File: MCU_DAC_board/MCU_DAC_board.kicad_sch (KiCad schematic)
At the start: 1 part, among them U1 ADAU1966AWBSTZ

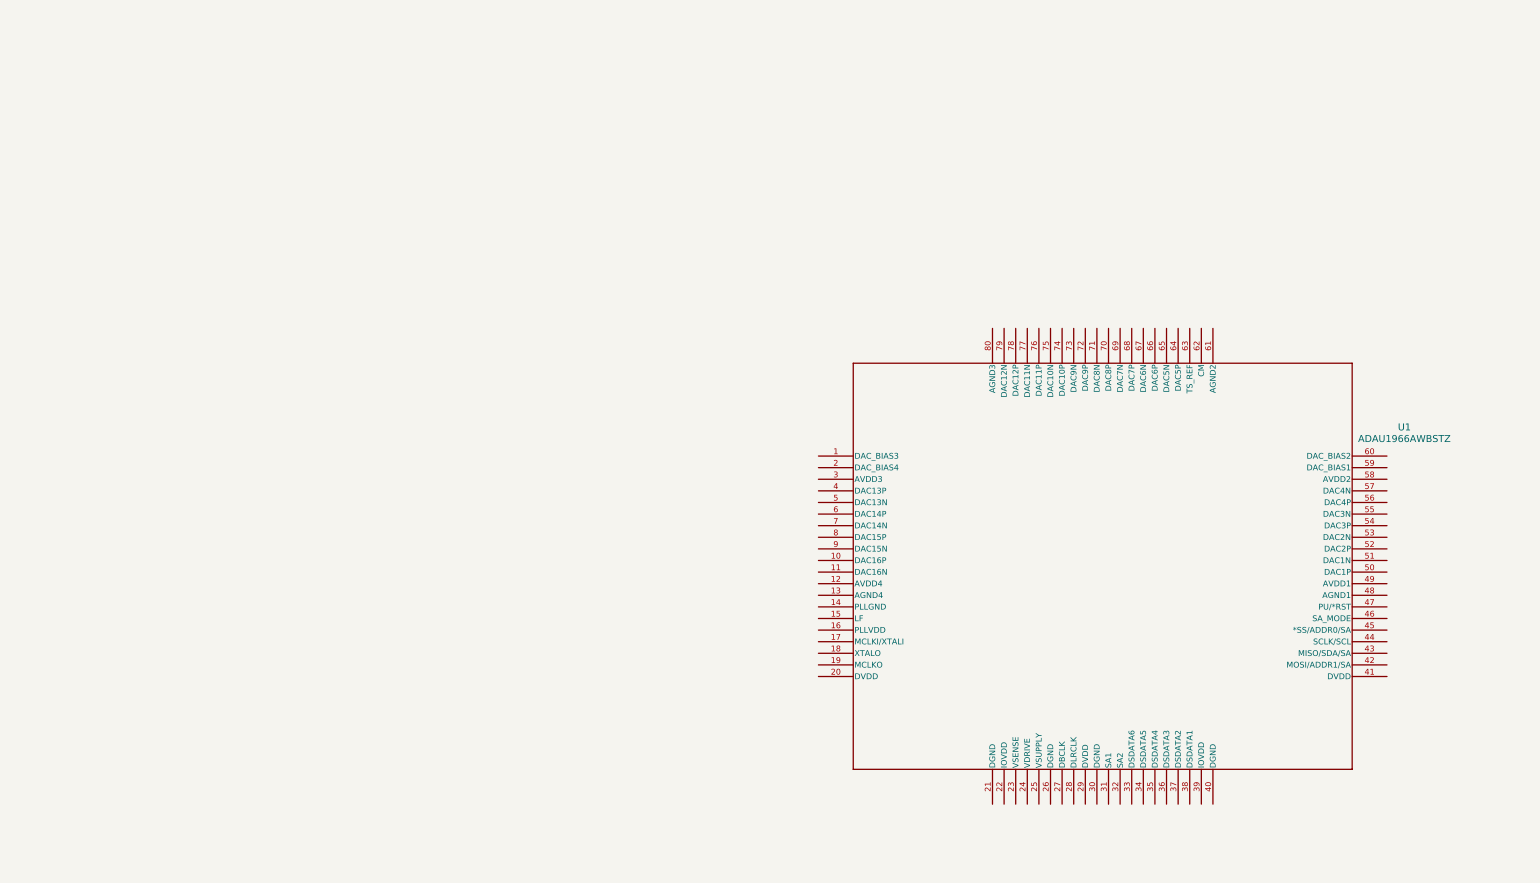
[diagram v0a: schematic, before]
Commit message: Added MCU dev board, connected power pins of DAC
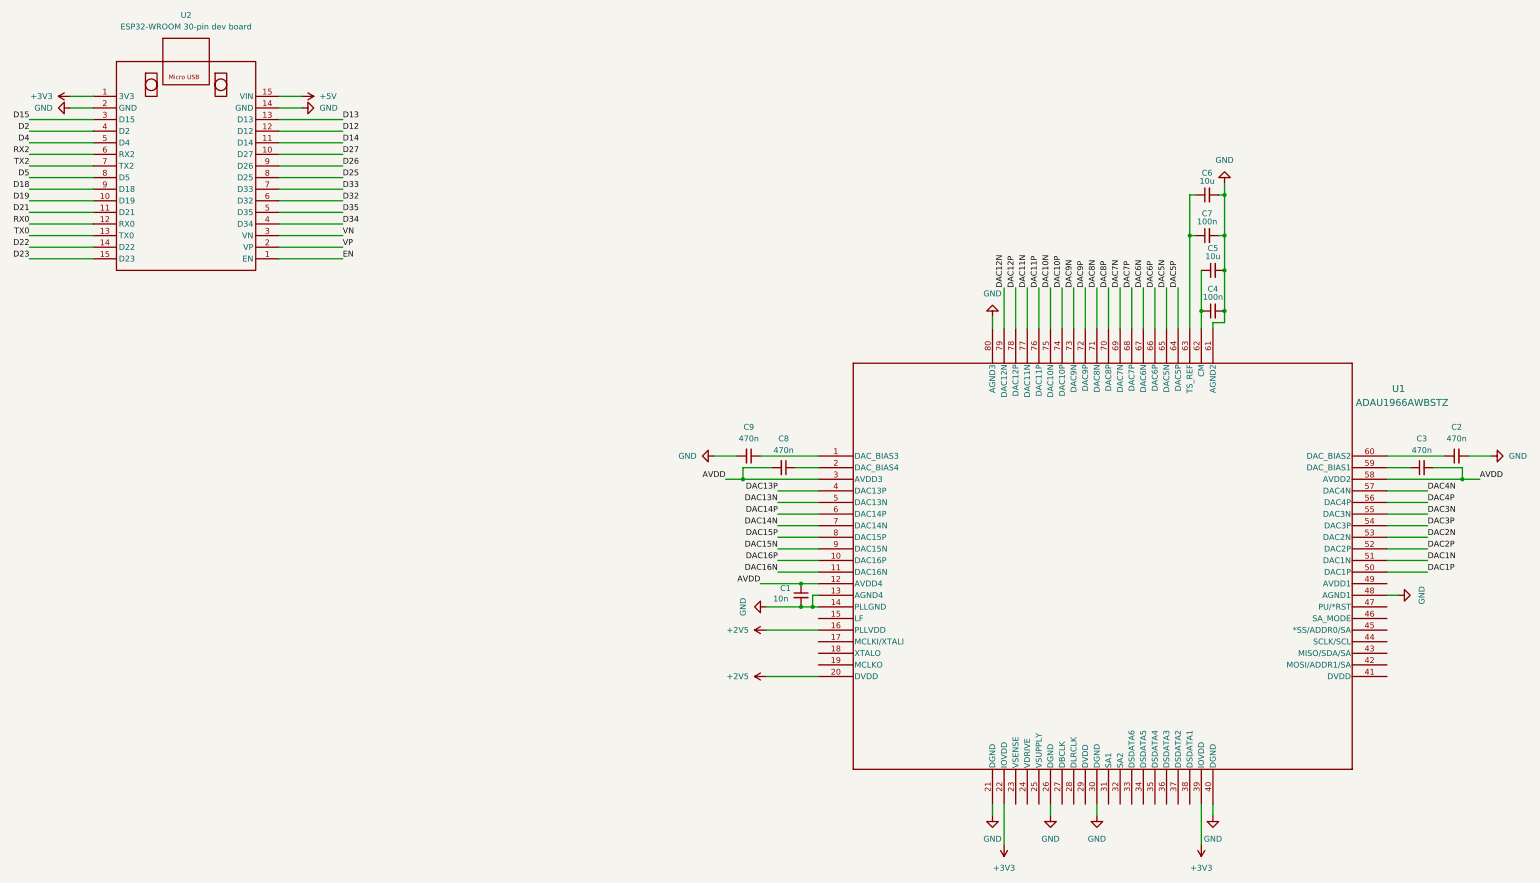
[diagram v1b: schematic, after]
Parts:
- added C1: 10n, symbol Device:C_Small
- added C2, C3, C8, C9: 470n, symbol Device:C_Small
- added C4, C7: 100n, symbol Device:C_Small
- added C5, C6: 10u, symbol Device:C_Small
- added U2: ESP32-WROOM 30-pin dev board, project_lib:ESP32-WROOM-30-DEVBOARD, symbol project_lib:ESP32-WROOM 30-pin dev board
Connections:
- net at U1.1 (DAC_BIAS3): now also C9.1
- net DAC16P: now reaches U1.10 (DAC16P)
- net DAC16N: now reaches U1.11 (DAC16N)
- net AVDD: now reaches U1.12 (AVDD4)
- net AVDD: now also U1.3 (AVDD3), U1.58 (AVDD2), C1.1, C3.2, C8.2
- net GND: now reaches U1.13 (AGND4)
- net GND: now also U1.14 (PLLGND), U1.21 (DGND), U1.26 (DGND), U1.30 (DGND), U1.40 (DGND), U1.48 (AGND1), U1.61 (AGND2), U1.80 (AGND3), C1.2, C2.2, C4.2, C5.2, C6.2, C7.2, C9.2, U2.14 (GND), U2.2 (VP)
- net +2V5: now reaches U1.16 (PLLVDD)
- net +2V5: now also U1.20 (DVDD)
- net at U1.2 (DAC_BIAS4): now also C8.1
- net +3V3: now reaches U1.22 (IOVDD)
- net +3V3: now also U1.39 (IOVDD), U2.1 (EN)
- net DAC13P: now reaches U1.4 (DAC13P)
- net DAC13N: now reaches U1.5 (DAC13N)
- net DAC1P: now reaches U1.50 (DAC1P)
- net DAC1N: now reaches U1.51 (DAC1N)
- net DAC2P: now reaches U1.52 (DAC2P)
- net DAC2N: now reaches U1.53 (DAC2N)
- net DAC3P: now reaches U1.54 (DAC3P)
- net DAC3N: now reaches U1.55 (DAC3N)
- net DAC4P: now reaches U1.56 (DAC4P)
- net DAC4N: now reaches U1.57 (DAC4N)
- net at U1.59 (DAC_BIAS1): now also C3.1
- net DAC14P: now reaches U1.6 (DAC14P)
- net at U1.60 (DAC_BIAS2): now also C2.1
- net at U1.62 (CM): now also C4.1, C5.1
- net at U1.63 (TS_REF): now also C6.1, C7.1
- net DAC5P: now reaches U1.64 (DAC5P)
- net DAC5N: now reaches U1.65 (DAC5N)
- net DAC6P: now reaches U1.66 (DAC6P)
- net DAC6N: now reaches U1.67 (DAC6N)
- net DAC7P: now reaches U1.68 (DAC7P)
- net DAC7N: now reaches U1.69 (DAC7N)
- net DAC14N: now reaches U1.7 (DAC14N)
- net DAC8P: now reaches U1.70 (DAC8P)
- net DAC8N: now reaches U1.71 (DAC8N)
- net DAC9P: now reaches U1.72 (DAC9P)
- net DAC9N: now reaches U1.73 (DAC9N)
- net DAC10P: now reaches U1.74 (DAC10P)
- net DAC10N: now reaches U1.75 (DAC10N)
- net DAC11P: now reaches U1.76 (DAC11P)
- net DAC11N: now reaches U1.77 (DAC11N)
- net DAC12P: now reaches U1.78 (DAC12P)
- net DAC12N: now reaches U1.79 (DAC12N)
- net DAC15P: now reaches U1.8 (DAC15P)
- net DAC15N: now reaches U1.9 (DAC15N)
- new net +5V: U2.15 (VIN)
- new net D12: U2.12 (RX0)
- new net D13: U2.13 (TX0)
- new net D14: U2.11 (D21)
- new net D15: U2.3 (VN)
- new net D18: U2.9 (D26)
- new net D19: U2.10 (D27)
- new net D2: U2.4 (D34)
- new net D21: U2.11 (D21)
- new net D22: U2.14 (GND)
- new net D23: U2.15 (VIN)
- new net D25: U2.8 (D5)
- new net D26: U2.9 (D26)
- new net D27: U2.10 (D27)
- new net D32: U2.6 (RX2)
- new net D33: U2.7 (TX2)
- new net D34: U2.4 (D34)
- new net D35: U2.5 (D4)
- new net D4: U2.5 (D4)
- new net D5: U2.8 (D5)
- new net EN: U2.1 (EN)
- new net RX0: U2.12 (RX0)
- new net RX2: U2.6 (RX2)
- new net TX0: U2.13 (TX0)
- new net TX2: U2.7 (TX2)
- new net VN: U2.3 (VN)
- new net VP: U2.2 (VP)

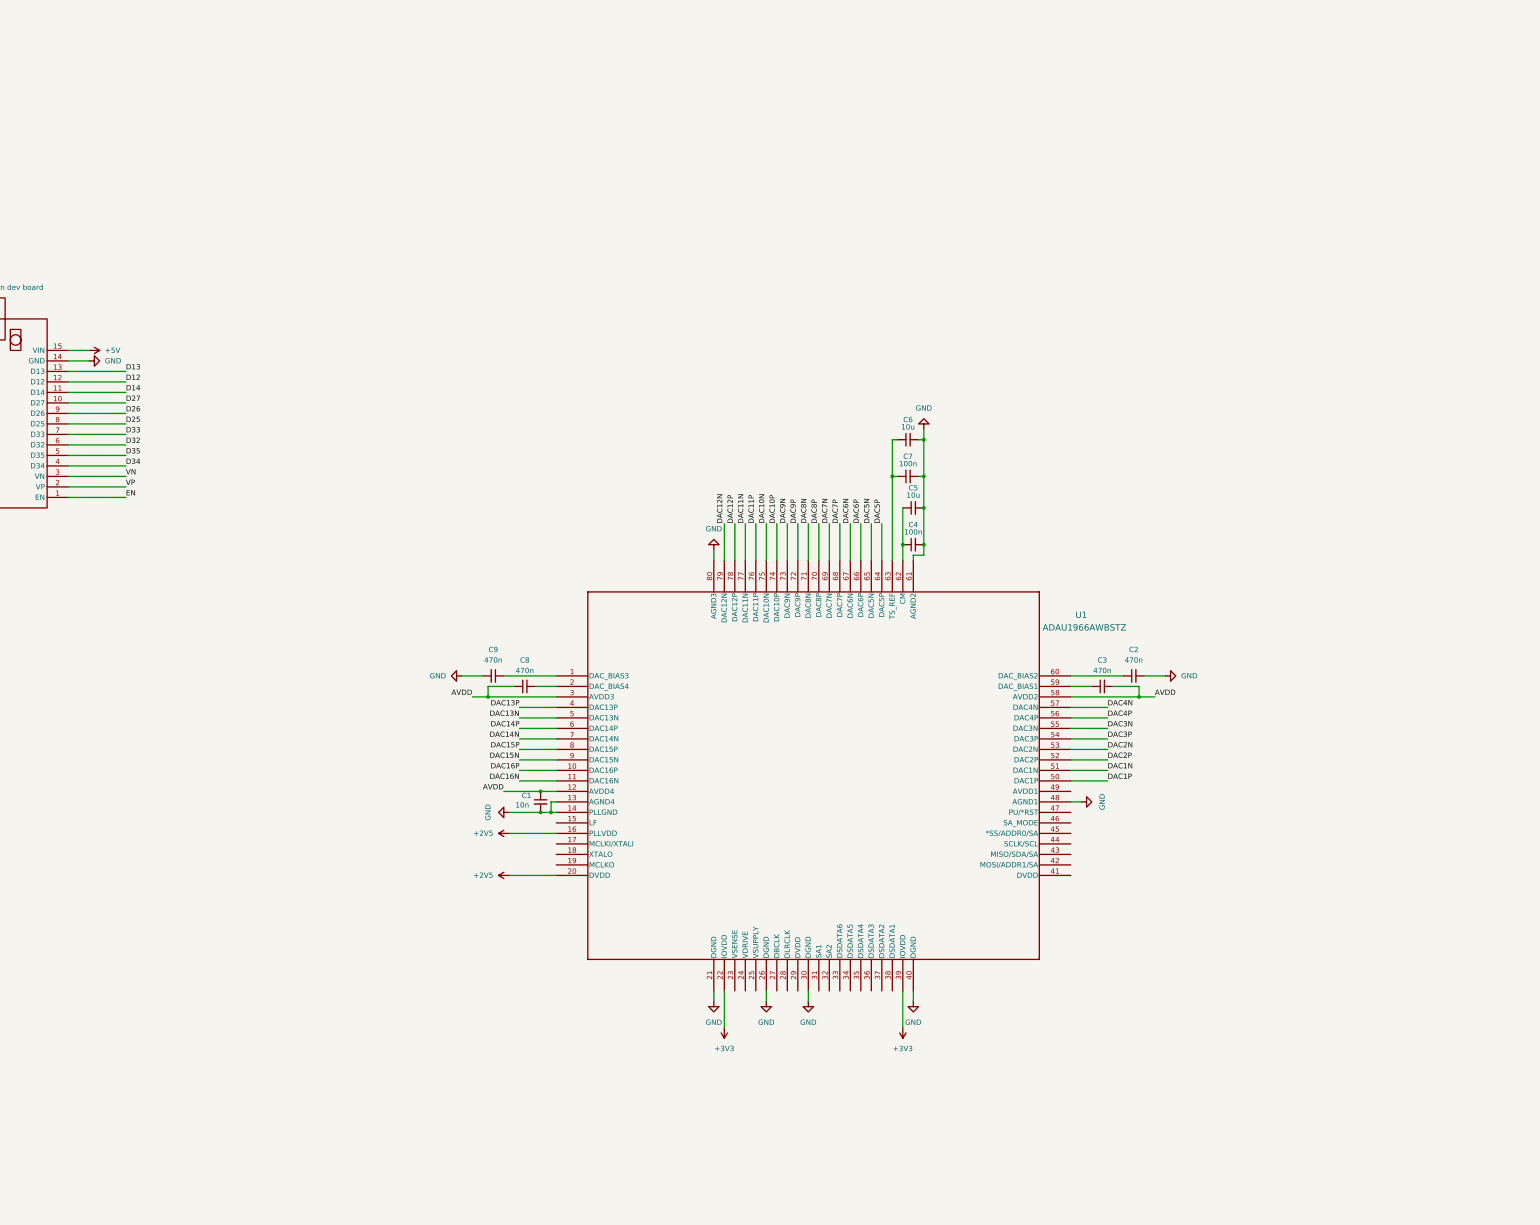
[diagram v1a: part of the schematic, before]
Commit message: Added buffers at DAC outputs
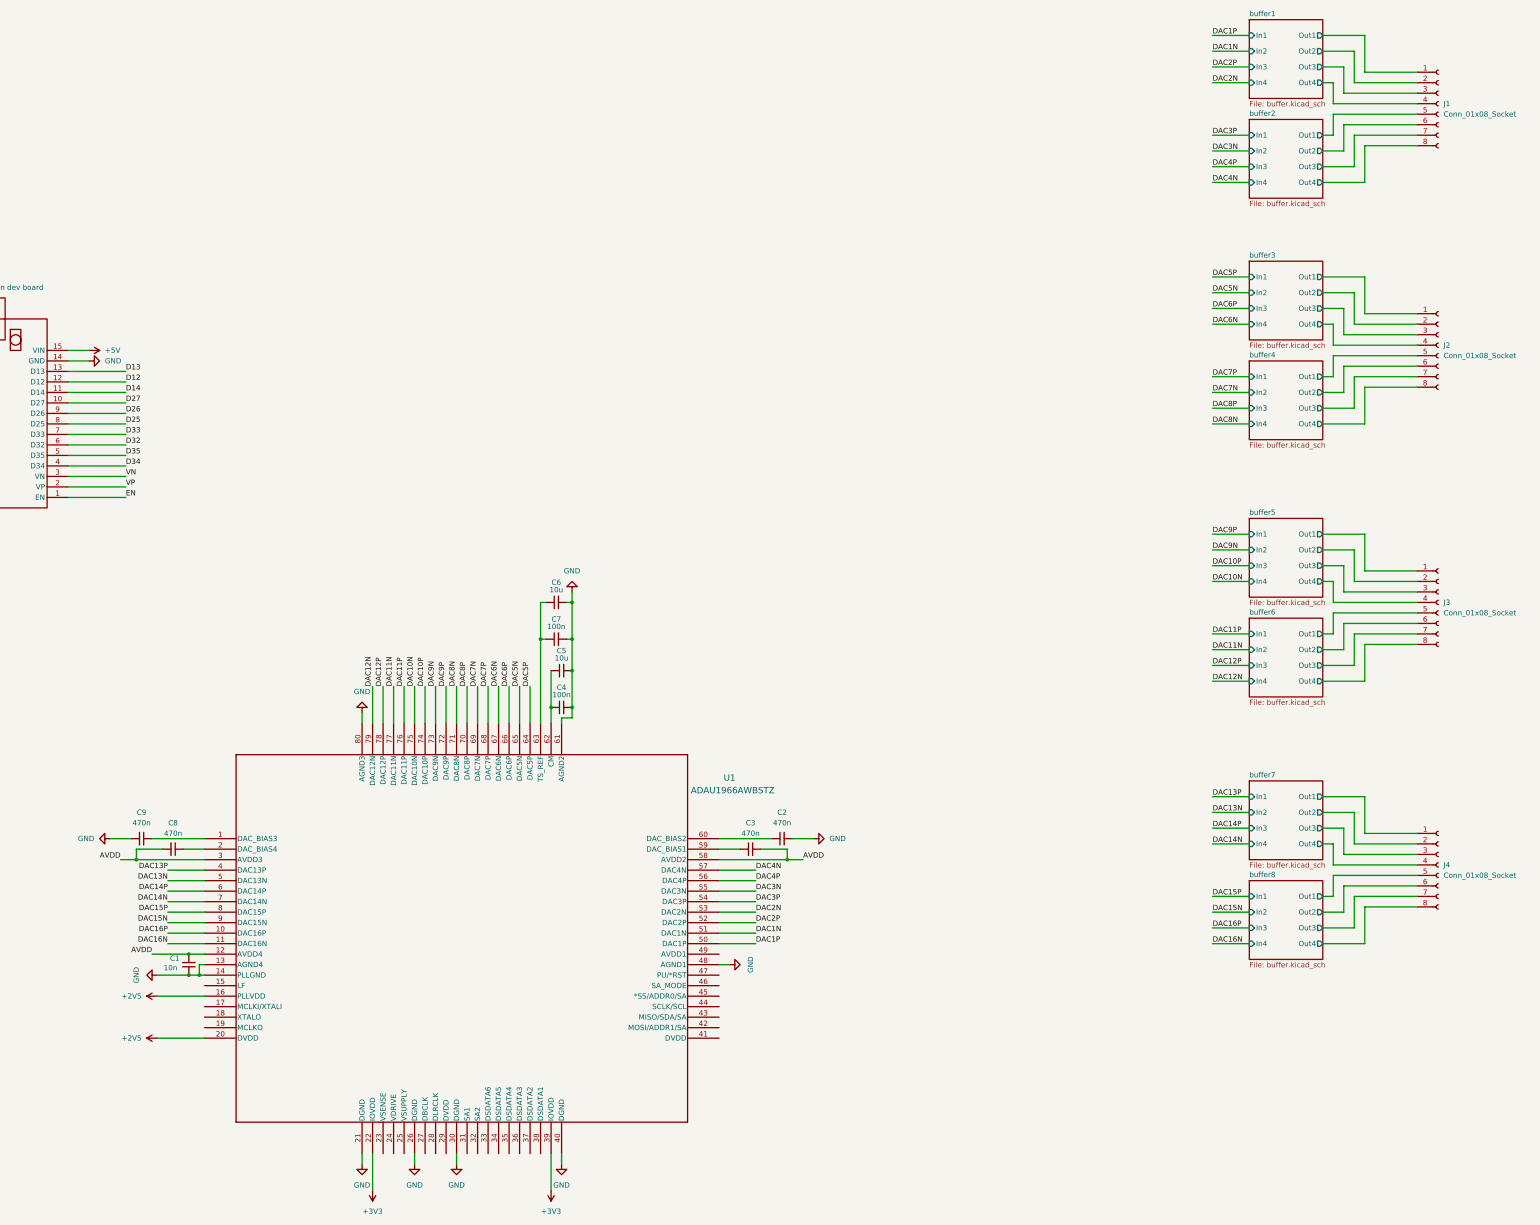
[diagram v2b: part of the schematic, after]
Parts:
- added J1, J2, J3, J4: Conn_01x08_Socket, symbol Connector:Conn_01x08_Socket
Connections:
- new net buffer1/Out1: J1.1 (Pin_1)
- new net buffer1/Out2: J1.2 (Pin_2)
- new net buffer1/Out3: J1.3 (Pin_3)
- new net buffer1/Out4: J1.4 (Pin_4)
- new net buffer2/Out1: J1.5 (Pin_5)
- new net buffer2/Out2: J1.6 (Pin_6)
- new net buffer2/Out3: J1.7 (Pin_7)
- new net buffer2/Out4: J1.8 (Pin_8)
- new net buffer3/Out1: J2.1 (Pin_1)
- new net buffer3/Out2: J2.2 (Pin_2)
- new net buffer3/Out3: J2.3 (Pin_3)
- new net buffer3/Out4: J2.4 (Pin_4)
- new net buffer4/Out1: J2.5 (Pin_5)
- new net buffer4/Out2: J2.6 (Pin_6)
- new net buffer4/Out3: J2.7 (Pin_7)
- new net buffer4/Out4: J2.8 (Pin_8)
- new net buffer5/Out1: J3.1 (Pin_1)
- new net buffer5/Out2: J3.2 (Pin_2)
- new net buffer5/Out3: J3.3 (Pin_3)
- new net buffer5/Out4: J3.4 (Pin_4)
- new net buffer6/Out1: J3.5 (Pin_5)
- new net buffer6/Out2: J3.6 (Pin_6)
- new net buffer6/Out3: J3.7 (Pin_7)
- new net buffer6/Out4: J3.8 (Pin_8)
- new net buffer7/Out1: J4.1 (Pin_1)
- new net buffer7/Out2: J4.2 (Pin_2)
- new net buffer7/Out3: J4.3 (Pin_3)
- new net buffer7/Out4: J4.4 (Pin_4)
- new net buffer8/Out1: J4.5 (Pin_5)
- new net buffer8/Out2: J4.6 (Pin_6)
- new net buffer8/Out3: J4.7 (Pin_7)
- new net buffer8/Out4: J4.8 (Pin_8)
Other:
- added sheet buffer1 (buffer.kicad_sch)
- added sheet buffer2 (buffer.kicad_sch)
- added sheet buffer3 (buffer.kicad_sch)
- added sheet buffer4 (buffer.kicad_sch)
- added sheet buffer5 (buffer.kicad_sch)
- added sheet buffer6 (buffer.kicad_sch)
- added sheet buffer7 (buffer.kicad_sch)
- added sheet buffer8 (buffer.kicad_sch)
- moved on the sheet: C1, C2, C3, C4, C5, C6, C7, C8, C9, U1
